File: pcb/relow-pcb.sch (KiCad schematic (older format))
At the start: 0 parts

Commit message: thermocouple circuit set up
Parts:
- added C?: 0.1uF, ~, symbol C
- added C?: 10uF, ~, symbol C
- added C? (x2): 1uF, ~, symbol C
- added IC?: AD8495, symbol AD849X
- added J?: TOASTER, ~, symbol 2PIN_FEMALE
- added K?: S212S01, ~, symbol SX12S01
- added R? (x2): 4.7kΩ, ~, symbol R
- added R?: 1MΩ, ~, symbol R
- added TC?: THERMOCOUPLE, symbol THERMOCOUPLE
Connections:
- new net: J?.1, K?.2 (OUT1)
- new net: J?.2, K?.1 (OUT2)
- new net: C?.1, C?.2, IC?.1 (-IN), R?.2
- new net: C?.1, C?.2, IC?.8 (+IN), R?.2
- new net: R?.1, TC?.1 (T+)
- new net: R?.1, R?.2, TC?.2 (T-)
- new net GND: C?.1, C?.1, C?.2, IC?.2 (REF), IC?.3 (-Vs), R?.1
- new net TEMP: IC?.5 (SENSE), IC?.6 (OUT)
- new net VCC: C?.2, IC?.7 (+Vs)

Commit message: realy circuit done
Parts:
- added LED?: HOT, ~, symbol LED
- added Q?: 2N3904, symbol NPN-BJT
- added R?: 180Ω, ~, symbol R
- added R?: 1kΩ, ~, symbol R
- added R?: 4.7kΩ, ~, symbol R
- added R?: 10kΩ, ~, symbol R
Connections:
- net GND: now also Q?.1 (E), R?.1
- net VCC: now also LED?.2 (A), R?.1
- net at K?.3 (IN+): now also R?.2
- net at K?.4 (IN-): now also Q?.3 (C), R?.2
- new net: Q?.2 (B), R?.2, R?.2
- new net: LED?.1 (C), R?.1
- new net HEAT: R?.1
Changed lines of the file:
@@
 Wire Wire Line
 	8100 2900 8000 2900
+$Comp
+L R R?
+U 1 1 5275EEF2
+P 2950 4100
+F 0 "R?" H 2800 4200 60  0000 C CNN
+F 1 "180Ω" H 3050 4200 60  0000 C CNN
+F 2 "~" H 2950 4100 60  0000 C CNN
+F 3 "~" H 2950 4100 60  0000 C CNN
+	1    2950 4100
+	1    0    0    -1
+$EndComp
+$Comp
+L VCC #PWR?
+U 1 1 5275EF1A
+P 2700 4100
+F 0 "#PWR?" H 2700 4200 30  0001 C CNN
+F 1 "VCC" H 2700 4200 30  0000 C CNN
+F 2 "" H 2700 4100 60  0000 C CNN
+F 3 "" H 2700 4100 60  0000 C CNN
+	1    2700 4100
+	0    -1   -1   0
+$EndComp
+Wire Wire Line
+	3100 4100 3200 4100
+$Comp
+L NPN-BJT Q?
+U 1 1 5275F500
+P 2950 4500
+F 0 "Q?" H 2950 4350 60  0000 C CNN
+F 1 "2N3904" H 3050 4250 60  0000 C CNN
+F 2 "" H 2950 4500 60  0000 C CNN
+F 3 "" H 2950 4500 60  0000 C CNN
+	1    2950 4500
+	1    0    0    -1
+$EndComp
+$Comp
+L R R?
+U 1 1 5275F634
+P 2950 4350
+F 0 "R?" H 2800 4450 60  0000 C CNN
+F 1 "1kΩ" H 3000 4450 60  0000 C CNN
+F 2 "~" H 2950 4350 60  0000 C CNN
+F 3 "~" H 2950 4350 60  0000 C CNN
+	1    2950 4350
+	1    0    0    -1
+$EndComp
+$Comp
+L LED LED?
+U 1 1 5275F6C0
+P 2550 4350
+F 0 "LED?" H 2400 4500 50  0000 C CNN
+F 1 "HOT" H 2400 4400 50  0000 C CNN
+F 2 "~" H 2550 4350 60  0000 C CNN
+F 3 "~" H 2550 4350 60  0000 C CNN
+	1    2550 4350
+	1    0    0    -1
+$EndComp
+$Comp
+L VCC #PWR?
+U 1 1 5275F6DE
+P 2300 4350
+F 0 "#PWR?" H 2300 4450 30  0001 C CNN
+F 1 "VCC" H 2300 4450 30  0000 C CNN
+F 2 "" H 2300 4350 60  0000 C CNN
+F 3 "" H 2300 4350 60  0000 C CNN
+	1    2300 4350
+	0    -1   -1   0
+$EndComp
+Wire Wire Line
+	2700 4100 2800 4100
+Wire Wire Line
+	3200 4200 3150 4200
+Wire Wire Line
+	3150 4200 3150 4450
+Wire Wire Line
+	3150 4450 3100 4450
+Wire Wire Line
+	3100 4350 3150 4350
+Connection ~ 3150 4350
+Wire Wire Line
+	2700 4350 2800 4350
+$Comp
+L GND #PWR?
+U 1 1 5275F7C8
+P 3200 4550
+F 0 "#PWR?" H 3200 4550 30  0001 C CNN
+F 1 "GND" H 3200 4480 30  0001 C CNN
+F 2 "" H 3200 4550 60  0000 C CNN
+F 3 "" H 3200 4550 60  0000 C CNN
+	1    3200 4550
+	0    -1   -1   0
+$EndComp
+Wire Wire Line
+	3200 4550 3100 4550
+$Comp
+L R R?
+U 1 1 5275F830
+P 2500 4500
+F 0 "R?" H 2300 4400 60  0000 C CNN
+F 1 "4.7kΩ" H 2550 4400 60  0000 C CNN
+F 2 "~" H 2500 4500 60  0000 C CNN
+F 3 "~" H 2500 4500 60  0000 C CNN
+	1    2500 4500
+	1    0    0    -1
+$EndComp
+$Comp
+L R R?
+U 1 1 5275F89E
+P 2500 4700
+F 0 "R?" H 2300 4600 60  0000 C CNN
+F 1 "10kΩ" H 2550 4600 60  0000 C CNN
+F 2 "~" H 2500 4700 60  0000 C CNN
+F 3 "~" H 2500 4700 60  0000 C CNN
+	1    2500 4700
+	1    0    0    -1
+$EndComp
+Wire Wire Line
+	2650 4500 2800 4500
+Wire Wire Line
+	2650 4700 2750 4700
+Wire Wire Line
+	2750 4700 2750 4500
+Connection ~ 2750 4500
+Wire Wire Line
+	1900 4500 2350 4500
+$Comp
+L GND #PWR?
+U 1 1 5275FA8A
+P 2200 4700
+F 0 "#PWR?" H 2200 4700 30  0001 C CNN
+F 1 "GND" H 2200 4630 30  0001 C CNN
+F 2 "" H 2200 4700 60  0000 C CNN
+F 3 "" H 2200 4700 60  0000 C CNN
+	1    2200 4700
+	0    1    1    0
+$EndComp
+Wire Wire Line
+	2200 4700 2350 4700
+Wire Wire Line
+	2300 4350 2400 4350
+Text Label 1900 4500 0    60   ~ 0
+HEAT
 $EndSCHEMATC

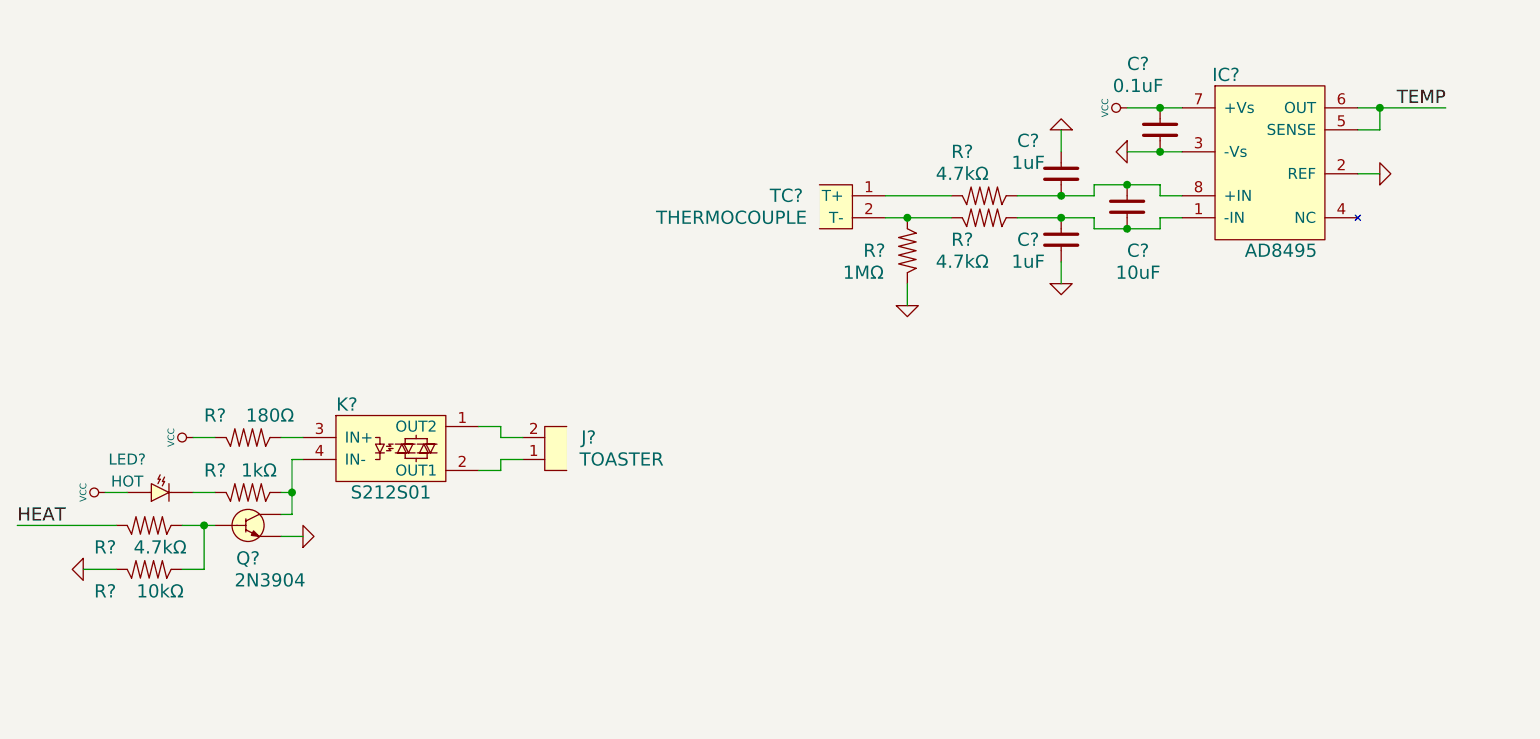
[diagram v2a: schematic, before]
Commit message: added rotary encoder
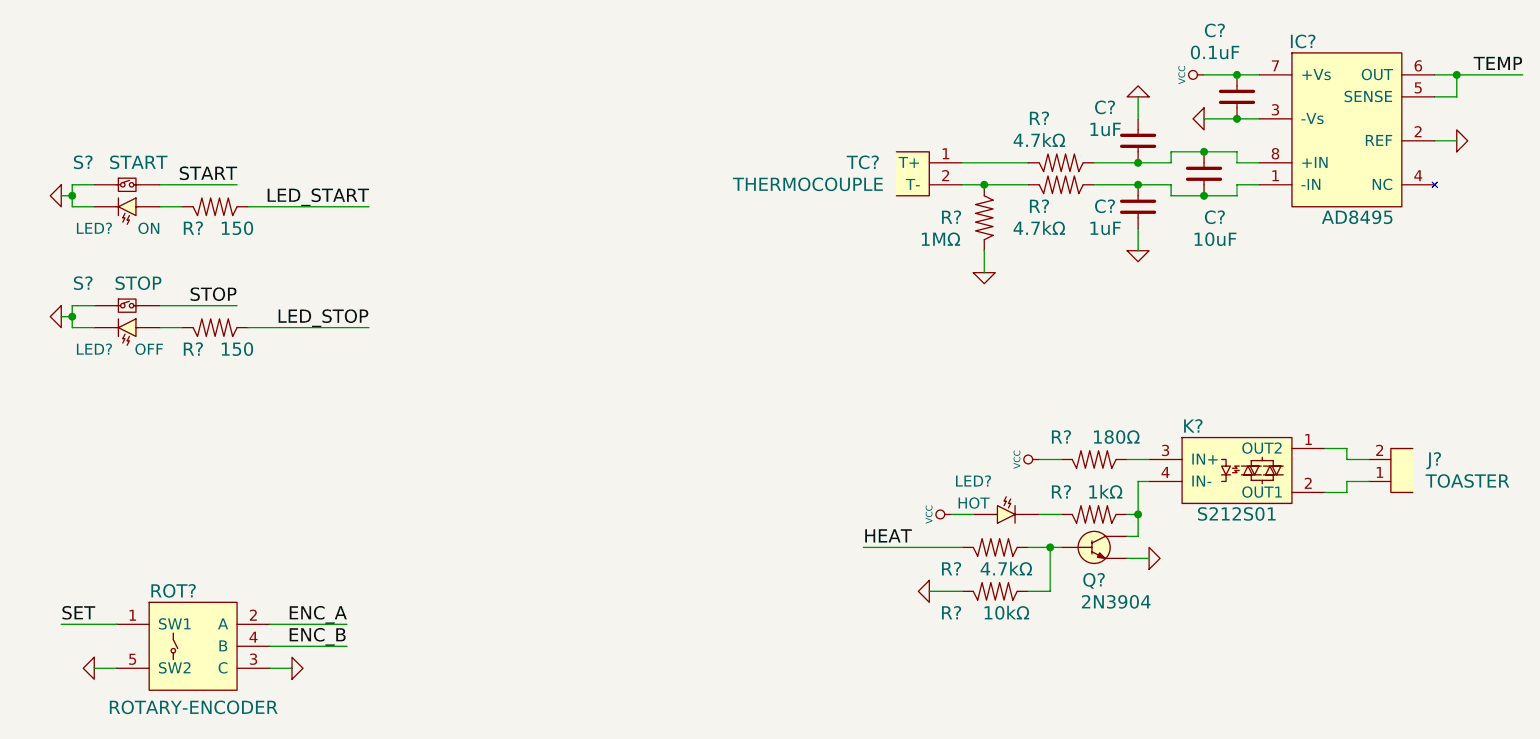
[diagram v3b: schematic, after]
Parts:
- added LED?: ON, ~, symbol LED
- added LED?: OFF, ~, symbol LED
- added R? (x2): 150, ~, symbol R
- added ROT?: ROTARY-ENCODER, symbol ROTARY-ENCODER
- added S?: START, ~, symbol SPST
- added S?: STOP, ~, symbol SPST
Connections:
- net GND: now also LED?.1 (C), LED?.1 (C), ROT?.3 (C), ROT?.5 (SW2), S?.1, S?.1
- new net: LED?.2 (A), R?.1 (x2)
- new net ENC_A: ROT?.2 (A)
- new net ENC_B: ROT?.4 (B)
- new net LED_START: R?.2
- new net LED_STOP: R?.2
- new net SET: ROT?.1 (SW1)
- new net START: S?.2
- new net STOP: S?.2
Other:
- moved on the sheet: C?, IC?, J?, K?, LED?, Q?, R?, TC?

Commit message: added a display
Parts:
- added LED?: 7-SEG_4-NUM-DISPLAY, symbol 7-SEG_4-NUM-DISPLAY
- added Q? (x4): MMBT4401, symbol NPN-BJT
- added R? (x8): 180Ω, ~, symbol R
- added R? (x4): 1kΩ, ~, symbol R
- added R? (x4): 10kΩ, ~, symbol R
- Q?: value 2N3904 -> MMBT4401; Manufacturer (none) -> ON Semiconductor; Part (none) -> MMBT4401LT1G
- R?: value 4.7kΩ -> 2.2kΩ
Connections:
- net GND: now also Q?.1 (E), Q?.1 (E), Q?.1 (E), Q?.1 (E), R?.2, R?.2, R?.2, R?.2
- new net: LED?.1 (E), R?.2
- new net: LED?.10 (F), R?.2
- new net: LED?.11 (A), R?.2
- new net: LED?.12 (COM1), Q?.3 (C)
- new net: LED?.2 (D), R?.2
- new net: LED?.3 (DP), R?.2
- new net: LED?.4 (C), R?.2
- new net: LED?.5 (G), R?.2
- new net: LED?.6 (COM4), Q?.3 (C)
- new net: LED?.7 (B), R?.2
- new net: LED?.8 (COM3), Q?.3 (C)
- new net: LED?.9 (COM2), Q?.3 (C)
- new net: Q?.2 (B), R?.1, R?.1 (x4)
- new net DIG1: R?.2
- new net DIG2: R?.2
- new net DIG3: R?.2
- new net DIG4: R?.2
- new net SEGA: R?.1
- new net SEGB: R?.1
- new net SEGC: R?.1
- new net SEGD: R?.1
- new net SEGDP: R?.1
- new net SEGE: R?.1
- new net SEGF: R?.1
- new net SEGG: R?.1

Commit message: initial pass at schematic done
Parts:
- added C? (x4): 0.1uF, ~, symbol C
- added IC?: ATMEGA328P_TQFP, ~, symbol ATMEGA328P_TQFP
- added P?: SERIAL, ~, symbol 6PIN_HEADER
- added P?: AVR_ISP, ~, symbol AVR_ISP
- added R? (x5): 10kΩ_opt, ~, symbol R
- R? (x2): value 150 -> 180Ω
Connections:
- net DIG1: now also IC?.23 (PC0(ADC0/PCINT8))
- net DIG2: now also IC?.24 (PC1(ADC1/PCINT9))
- net DIG3: now also IC?.25 (PC2(ADC2/PCINT10))
- net DIG4: now also IC?.26 (PC3(ADC3/PCINT11))
- net ENC_A: now also IC?.27 (PC4(ADC4/SDA/PCINT12)), R?.1
- net ENC_B: now also IC?.28 (PC5(ADC5/SCL/PCINT13)), R?.1
- net GND: now also C?.1, C?.1, C?.1, C?.1, IC?.21 (GND), IC?.3 (GND), IC?.5 (GND), P?.1, P?.2, P?.6 (GND)
- net HEAT: now also IC?.11 (PD7(PCINT23/AIN1))
- net LED_START: now also IC?.9 (PD5(PCINT21/OC0B/T1))
- net LED_STOP: now also IC?.10 (PD6(PCINT22/OC0A/AIN0))
- net SEGA: now also IC?.12 (PB0(PCINT0/CLKO/ICP1))
- net SEGB: now also IC?.13 (PB1(PCINT1/OC1A))
- net SEGC: now also IC?.14 (PB2(PCINT2/~SS~/OC1B))
- net SEGDP: now also IC?.8 (XTAL2(PB7))
- net SEGG: now also IC?.7 (XTAL1(PB6))
- net SET: now also IC?.2 (PD4(PCINT20/XCK/T0)), R?.1
- net START: now also IC?.32 (PD2(INT0/PCINT18)), R?.1
- net STOP: now also IC?.1 (PD3(PCINT19/OC2B/INT1)), R?.1
- net TEMP: now also IC?.22 (ADC7)
- net VCC: now also C?.2, C?.2, C?.2, C?.2, IC?.18 (AVCC), IC?.20 (AREF), IC?.4 (VCC), IC?.6 (VCC), P?.2 (VCC), P?.3, R?.2, R?.2, R?.2, R?.2, R?.2
- net SEGD renamed MOSI
- net MOSI: now also IC?.15 (PB3(PCINT3/OC2A/MOSI)), P?.4 (MOSI)
- net SEGE renamed MISO
- net MISO: now also IC?.16 (PB4(PCINT4/MISO)), P?.1 (MISO)
- net SEGF renamed SCK
- net SCK: now also IC?.17 (PB5(SCK/PCINT5)), P?.3 (SCK)
- new net RESET: IC?.29 (~RESET~(PC6)), P?.5 (RESET), P?.6
- new net USART_RX: IC?.30 (PD0(RXD/PCINT16)), P?.4
- new net USART_TX: IC?.31 (PD1(TXD/PCINT17)), P?.5
- no-connect marks 0 -> 1
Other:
- note added: "AC RELAY"
- note added: "DISPLAY"
- note added: "MCU"
- note added: "PROGRAMMING AND DEBUGGING"
- note added: "SET TEMPERATURE INPUT"
- note added: "SWITCH INPUTS"
- note added: "THERMOCOUPLE INPUT"
- moved on the sheet: C?, IC?, J?, K?, LED?, Q?, R?, ROT?, S?, TC?

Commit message: I lied. Adding a FTDI USB to USART
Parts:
- added C?: 10nF, ~, symbol C
- added F?: PTC, ~, symbol PTC
- added IC?: FT230X_SOP, ~, symbol FT230X_SOP
- added J?: MICROUSB, ~, symbol MICROUSB
- gave numbers to parts that had none: 57
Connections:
- net GND: now also C?.2, J?.5 (GND)
- new net: C?.1, J?.1 (VBUS)
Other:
- moved on the sheet: P1, P2

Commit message: might actually be done with this schematic
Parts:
- removed P1: SERIAL, ~, symbol 6PIN_HEADER
- added C10, C9: 0.1uF, ~, symbol C
- added C12, C13: 47nF, ~, symbol C
- added LED1: TXLED, ~, symbol LED
- added LED2: RXLED, ~, symbol LED
- added R1: 10kΩ_opt, ~, symbol R
- added R5, R6: 330Ω, ~, symbol R
- added R7, R8: 27Ω, ~, symbol R
- C11: renamed from C?; value 10nF -> 10uF
- F1: renamed from F?; value PTC -> 500mA
- gave numbers to parts that had none: 2
- renumbered C5 to C3, C3 to C4, C4 to C5, J1 to J2, LED2 to LED3, LED3 to LED4, LED1 to LED5, LED4 to LED6, P2 to P1, Q2 to Q1, Q1 to Q2, R13 to R10, R14 to R11, R8 to R12, R9 to R13, R10 to R14, R11 to R15, R1 to R16, R15 to R17, R2 to R18, R16 to R19, R3 to R2, R4 to R20, R17 to R21, R18 to R22, R7 to R23, R19 to R24, R20 to R25, R21 to R26, R22 to R27, R23 to R28, R24 to R29, R5 to R3, R25 to R30, R26 to R31, R27 to R32, R28 to R33, R29 to R34, R30 to R35, R6 to R4, R12 to R9
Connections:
- net GND: now also IC3.13 (GND), IC3.5 (GND), IC3.6 (~CTS~), Q2.3 (C), R23.2, C10.1, C12.1, C13.1, C9.1; no longer Q2.1 (E), R23.1
- net HEAT: now also R20.2; no longer R20.1
- net RESET: now also IC3.2 (~RTS~), R1.2
- net USART_RX: now also IC3.1 (TXD)
- net USART_TX: now also IC3.4 (RXD)
- net VCC: now also F1.2, IC3.12 (VCC), C10.2, R1.1, R5.2, R6.2
- net at K1.4 (IN-), R18.2: now also Q2.1 (E); no longer Q2.3 (C)
- net at C11.1, J1.1 (VBUS): now also F1.1
- net at J1.2 (D-): now also C12.2, R7.1
- net at J1.3 (D+): now also C13.2, R8.1
- net at IC3.10 (3V3OUT): now also IC3.11 (~RESET~), IC3.3 (VCCIO), C9.2
- net at IC3.14 (CBUS1): now also LED1.1 (C)
- net at IC3.7 (CBUS2): now also LED2.1 (C)
- net at IC3.8 (USBDP): now also R8.2
- net at IC3.9 (USBDM): now also R7.2
- new net: Q2.2 (B), R20.1, R23.1
- new net: LED1.2 (A), R5.1
- new net: LED2.2 (A), R6.1
- no-connect marks 1 -> 3
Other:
- moved on the sheet: C1, C11, C2, C3, C4, C5, C6, C7, C8, F1, IC1, IC2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

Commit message: footprint assignment almost done. going to bed
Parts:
- removed Q1, Q2, Q3, Q4, Q5: MMBT4401, symbol NPN-BJT
- added Q1, Q2, Q3, Q4, Q5: MMBT4401, ~, symbol NPN-BJT_SOT
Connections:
- net GND: now also Q1.2 (E), Q2.3 (C), Q3.2 (E), Q4.2 (E), Q5.2 (E)
- net at K1.4 (IN-), R18.2: now also Q2.2 (E)
- net at R20.1, R23.1: now also Q2.1 (B)
- net at LED6.12 (COM1): now also Q1.3 (C)
- net at LED6.6 (COM4): now also Q5.3 (C)
- net at LED6.8 (COM3): now also Q4.3 (C)
- net at LED6.9 (COM2): now also Q3.3 (C)
- net at R17.1, R19.1: now also Q1.1 (B)
- net at R22.1, R25.1: now also Q3.1 (B)
- net at R29.1, R31.1: now also Q4.1 (B)
- net at R34.1, R35.1: now also Q5.1 (B)
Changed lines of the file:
@@
 	8250 5600 8350 5600
-$Comp
-L NPN-BJT Q2
-U 1 1 5275F500
-P 8700 6050
-F 0 "Q2" H 8800 6200 60  0000 C CNN
-F 1 "MMBT4401" H 8800 6300 60  0000 C CNN
-F 2 "" H 8700 6050 60  0000 C CNN
-F 3 "" H 8700 6050 60  0000 C CNN
-F 4 "ON Semiconductor" H 8700 6050 60  0001 C CNN "Manufacturer"
-F 5 "MMBT4401LT1G" H 8700 6050 60  0001 C CNN "Part"
-	1    8700 6050
-	-1   0    0    1
-$EndComp
 $Comp
 L R R18
@@
 	2250 6950 2350 6950
 $Comp
-L NPN-BJT Q1
-U 1 1 52768E10
-P 3750 5950
-F 0 "Q1" H 3650 5850 60  0000 C CNN
-F 1 "MMBT4401" H 3850 6100 60  0000 C CNN
-F 2 "" H 3750 5950 60  0000 C CNN
-F 3 "" H 3750 5950 60  0000 C CNN
-F 4 "ON Semiconductor" H 3750 5950 60  0001 C CNN "Manufacturer"
-F 5 "MMBT4401LT1G" H 3750 5950 60  0001 C CNN "Part"
-	1    3750 5950
-	-1   0    0    1
-$EndComp
-$Comp
 L R R19
 U 1 1 52768E50
@@
 	1600 6950 1950 6950
 $Comp
-L NPN-BJT Q3
-U 1 1 52769259
-P 3750 6350
-F 0 "Q3" H 3650 6250 60  0000 C CNN
-F 1 "MMBT4401" H 3850 6500 60  0000 C CNN
-F 2 "" H 3750 6350 60  0000 C CNN
-F 3 "" H 3750 6350 60  0000 C CNN
-F 4 "ON Semiconductor" H 3750 6350 60  0001 C CNN "Manufacturer"
-F 5 "MMBT4401LT1G" H 3750 6350 60  0001 C CNN "Part"
-	1    3750 6350
-	-1   0    0    1
-$EndComp
-$Comp
 L R R25
 U 1 1 5276925F
@@
 	4700 6350 4300 6350
 $Comp
-L NPN-BJT Q4
-U 1 1 527692D0
-P 3750 6750
-F 0 "Q4" H 3650 6650 60  0000 C CNN
-F 1 "MMBT4401" H 3850 6900 60  0000 C CNN
-F 2 "" H 3750 6750 60  0000 C CNN
-F 3 "" H 3750 6750 60  0000 C CNN
-F 4 "ON Semiconductor" H 3750 6750 60  0001 C CNN "Manufacturer"
-F 5 "MMBT4401LT1G" H 3750 6750 60  0001 C CNN "Part"
-	1    3750 6750
-	-1   0    0    1
-$EndComp
-$Comp
 L R R31
 U 1 1 527692D6
@@
 Wire Wire Line
 	4700 6750 4300 6750
-$Comp
-L NPN-BJT Q5
-U 1 1 527692F1
-P 3750 7150
-F 0 "Q5" H 3650 7050 60  0000 C CNN
-F 1 "MMBT4401" H 3850 7300 60  0000 C CNN
-F 2 "" H 3750 7150 60  0000 C CNN
-F 3 "" H 3750 7150 60  0000 C CNN
-F 4 "ON Semiconductor" H 3750 7150 60  0001 C CNN "Manufacturer"
-F 5 "MMBT4401LT1G" H 3750 7150 60  0001 C CNN "Part"
-	1    3750 7150
-	-1   0    0    1
-$EndComp
 $Comp
 L R R35
@@
 Wire Wire Line
 	1300 3050 1300 2950
+$Comp
+L NPN-BJT_SOT Q1
+U 1 1 52776182
+P 3750 5950
+F 0 "Q1" H 3650 5850 60  0000 C CNN
+F 1 "MMBT4401" H 3800 6100 60  0000 C CNN
+F 2 "~" H 3750 5950 60  0000 C CNN
+F 3 "~" H 3750 5950 60  0000 C CNN
+	1    3750 5950
+	-1   0    0    1
+$EndComp
+$Comp
+L NPN-BJT_SOT Q3
+U 1 1 527761B9
+P 3750 6350
+F 0 "Q3" H 3650 6250 60  0000 C CNN
+F 1 "MMBT4401" H 3800 6500 60  0000 C CNN
+F 2 "~" H 3750 6350 60  0000 C CNN
+F 3 "~" H 3750 6350 60  0000 C CNN
+	1    3750 6350
+	-1   0    0    1
+$EndComp
+$Comp
+L NPN-BJT_SOT Q4
+U 1 1 527761BF
+P 3750 6750
+F 0 "Q4" H 3650 6650 60  0000 C CNN
+F 1 "MMBT4401" H 3800 6900 60  0000 C CNN
+F 2 "~" H 3750 6750 60  0000 C CNN
+F 3 "~" H 3750 6750 60  0000 C CNN
+	1    3750 6750
+	-1   0    0    1
+$EndComp
+$Comp
+L NPN-BJT_SOT Q5
+U 1 1 527761C5
+P 3750 7150
+F 0 "Q5" H 3650 7050 60  0000 C CNN
+F 1 "MMBT4401" H 3800 7300 60  0000 C CNN
+F 2 "~" H 3750 7150 60  0000 C CNN
+F 3 "~" H 3750 7150 60  0000 C CNN
+	1    3750 7150
+	-1   0    0    1
+$EndComp
+$Comp
+L NPN-BJT_SOT Q2
+U 1 1 527761CB
+P 8700 6050
+F 0 "Q2" H 8600 5950 60  0000 C CNN
+F 1 "MMBT4401" H 8750 6200 60  0000 C CNN
+F 2 "~" H 8700 6050 60  0000 C CNN
+F 3 "~" H 8700 6050 60  0000 C CNN
+	1    8700 6050
+	-1   0    0    1
+$EndComp
 $EndSCHEMATC
